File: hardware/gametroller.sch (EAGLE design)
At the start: 48 parts, among them J1 microUSB, J2 PJ-002AH-SMT-TR, J3 USB-A, SW1 SPST_TACT-KMR2, U1 LP5907MFX-3.3/NOPB, U16 AOZ1280CI, U2 TPS2115AIPWRQ1-SON8, U4 ATSAMD21G18_QFN, X2 32.768

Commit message: Minor modifications and cleanup to PCB
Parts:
- added F1: 500mA, gametroller:R-US_R0603
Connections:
- new net N$4: F1.1, J1.VBUS
- net VBUS: now also F1.2; no longer J1.VBUS
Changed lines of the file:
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@@
 <?xml version="1.0" encoding="utf-8"?>
 <!DOCTYPE eagle SYSTEM "eagle.dtd">
-<eagle version="9.1.0">
+<eagle version="9.1.3">
 <drawing>
 <settings>
@@
 <part name="SW1" library="gametroller" deviceset="SPST_TACT" device="-KMR2"/>
 <part name="+3V4" library="gametroller" deviceset="+3V3" device=""/>
-<part name="U$1" library="gametroller" deviceset="VBUS" device=""/>
 <part name="J1" library="gametroller" deviceset="USB-MICRO" device="" value="microUSB"/>
 <part name="U4" library="gametroller" deviceset="ATSAMD21J" device="_QFP" value="ATSAMD21G18_QFN"/>
@@
 <part name="R3" library="gametroller" deviceset="R-US_" device="R0603" value="1k"/>
 <part name="GND3" library="gametroller" deviceset="GND" device=""/>
+<part name="F1" library="gametroller" deviceset="R-US_" device="R0603" value="500mA">
+<attribute name="MFG" value="Bel Fuse Inc."/>
+<attribute name="MPN" value="0ZCK0050FF2E"/>
+<attribute name="PN-DK" value="507-1813-1-ND"/>
+</part>
+<part name="U$2" library="gametroller" deviceset="VBUS" device=""/>
 </parts>
 <sheets>
@@
 </instance>
 <instance part="+3V4" gate="G$1" x="66.04" y="147.32" rot="MR0"/>
-<instance part="U$1" gate="G$1" x="162.56" y="63.5"/>
 <instance part="J1" gate="G$1" x="149.86" y="53.34" rot="MR0"/>
 <instance part="U4" gate="G$1" x="60.96" y="60.96"/>
@@
 <instance part="R3" gate="G$1" x="213.36" y="60.96" rot="R270"/>
 <instance part="GND3" gate="G$1" x="213.36" y="40.64" rot="MR0"/>
+<instance part="F1" gate="G$1" x="165.1" y="58.42" smashed="yes">
+<attribute name="NAME" x="162.56" y="60.96" size="1.778" layer="95" align="center"/>
+<attribute name="VALUE" x="170.18" y="60.96" size="1.778" layer="96" align="center"/>
+<attribute name="MFG" x="165.1" y="58.42" size="1.778" layer="96" display="off"/>
+</instance>
+<instance part="U$2" gate="G$1" x="180.34" y="63.5"/>
 </instances>
 <busses>
@@
 <net name="VBUS" class="0">
 <segment>
-<wire x1="157.48" y1="58.42" x2="162.56" y2="58.42" width="0.1524" layer="91"/>
-<wire x1="162.56" y1="58.42" x2="162.56" y2="60.96" width="0.1524" layer="91"/>
-<pinref part="U$1" gate="G$1" pin="VBUS"/>
-<pinref part="J1" gate="G$1" pin="VBUS"/>
-<wire x1="162.56" y1="58.42" x2="180.34" y2="58.42" width="0.1524" layer="91"/>
-<junction x="162.56" y="58.42"/>
 <pinref part="C18" gate="G$1" pin="1"/>
+<wire x1="170.18" y1="58.42" x2="180.34" y2="58.42" width="0.1524" layer="91"/>
 <wire x1="180.34" y1="58.42" x2="180.34" y2="55.88" width="0.1524" layer="91"/>
+<pinref part="F1" gate="G$1" pin="2"/>
+<pinref part="U$2" gate="G$1" pin="VBUS"/>
+<wire x1="180.34" y1="58.42" x2="180.34" y2="60.96" width="0.1524" layer="91"/>
+<junction x="180.34" y="58.42"/>
 </segment>
 <segment>
@@
 <segment>
 <pinref part="J3" gate="G$1" pin="D+"/>
-<wire x1="160.02" y1="86.36" x2="170.18" y2="86.36" width="0.1524" layer="91"/>
-<label x="165.1" y="86.36" size="1.778" layer="95"/>
+<wire x1="160.02" y1="83.82" x2="170.18" y2="83.82" width="0.1524" layer="91"/>
+<label x="165.1" y="83.82" size="1.778" layer="95"/>
 </segment>
 </net>
@@
 <segment>
 <pinref part="J3" gate="G$1" pin="D-"/>
-<wire x1="160.02" y1="83.82" x2="170.18" y2="83.82" width="0.1524" layer="91"/>
-<label x="165.1" y="83.82" size="1.778" layer="95"/>
+<wire x1="160.02" y1="86.36" x2="170.18" y2="86.36" width="0.1524" layer="91"/>
+<label x="165.1" y="86.36" size="1.778" layer="95"/>
 </segment>
 </net>
@@
 </segment>
 </net>
+<net name="N$4" class="0">
+<segment>
+<pinref part="F1" gate="G$1" pin="1"/>
+<wire x1="157.48" y1="58.42" x2="160.02" y2="58.42" width="0.1524" layer="91"/>
+<pinref part="J1" gate="G$1" pin="VBUS"/>
+</segment>
+</net>

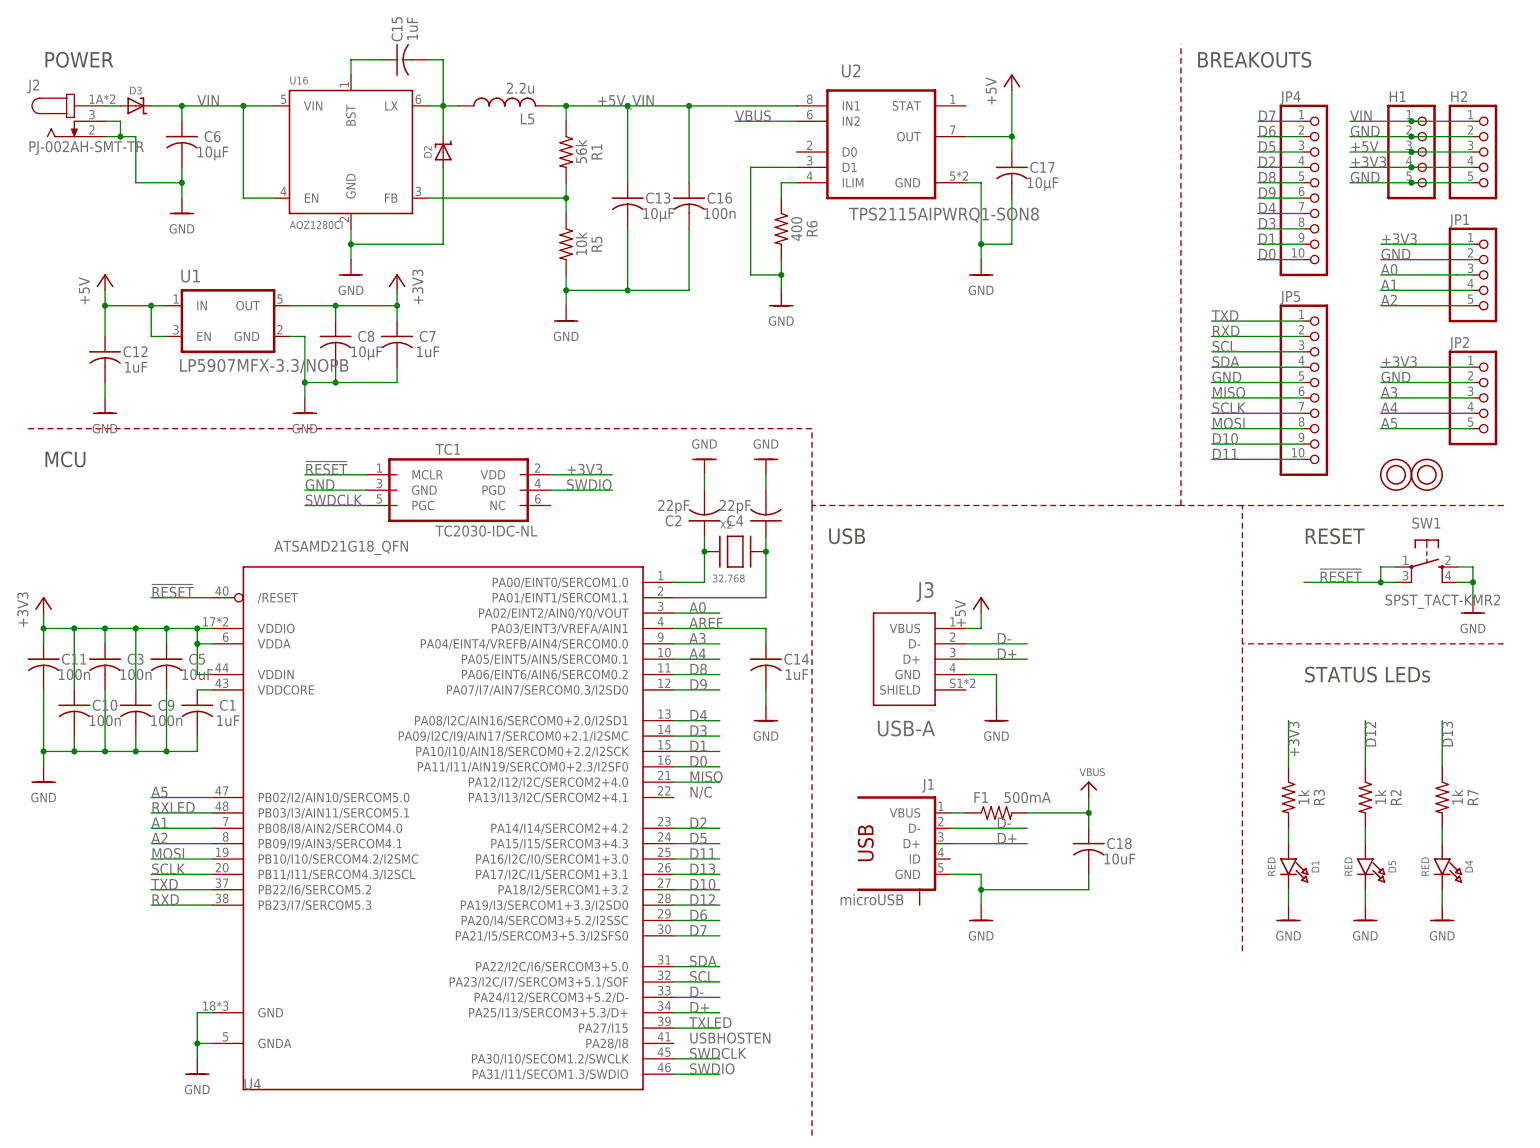
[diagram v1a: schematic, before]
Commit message: Added 22M pullup resistors to several IO pins to allow board to be used as a MaKeyMaKey clone
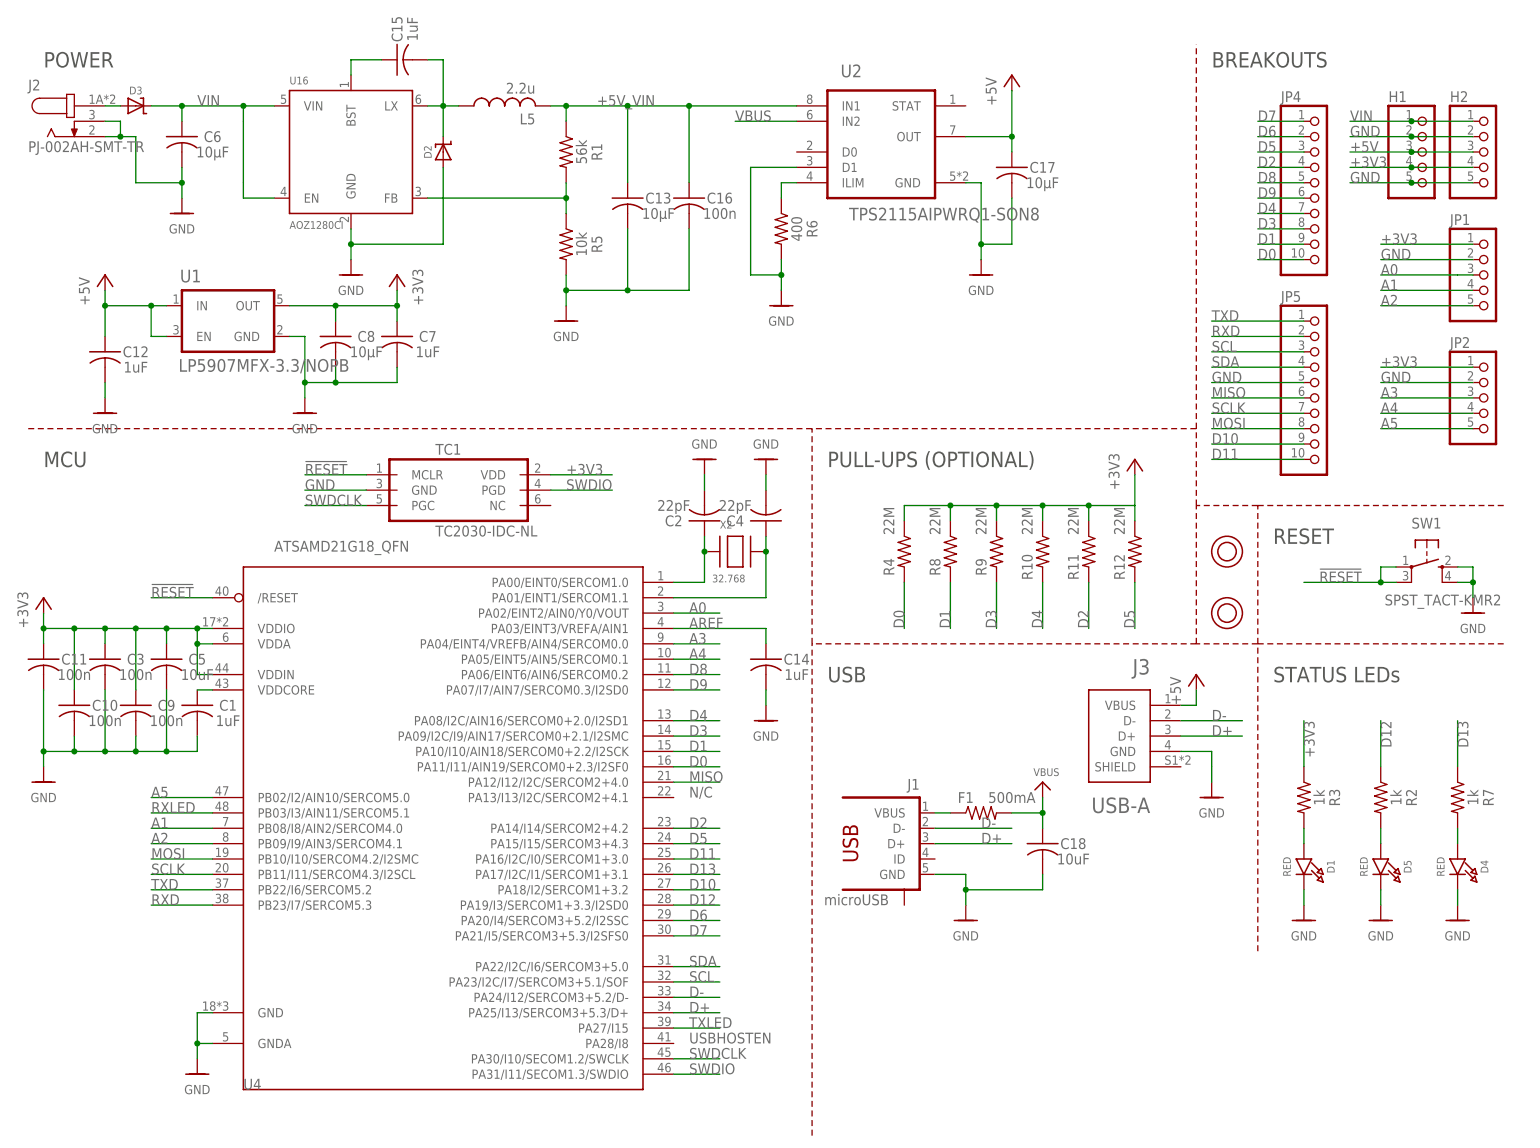
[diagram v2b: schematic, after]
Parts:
- added R10, R11, R12, R4, R8, R9: 22M, gametroller:R-US_R0603
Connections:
- net +3V3: now also R10.1, R11.1, R12.1, R4.1, R8.1, R9.1
- net D0: now also R4.2
- net D1: now also R8.2
- net D2: now also R11.2
- net D3: now also R9.2
- net D4: now also R10.2
- net D5: now also R12.2
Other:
- note added: "PULL-UPS (OPTIONAL)"
- moved on the sheet: C18, D1, D4, D5, F1, J1, J3, R2, R3, R7

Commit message: Updated BOM attributes for currently available parts
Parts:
- C1, C12, C14, C15, C7: MFG (none) -> AVX Corporation; MPN (none) -> 0603ZC105KAT2A; PN-DK (none) -> 478-7940-1-ND
- C10, C11, C16, C3, C9: MFG (none) -> KEMET; MPN (none) -> C0603X104K5RAC7867; PN-DK (none) -> 399-7969-1-ND
- C13, C17, C6, C8: value 10µF -> 10uF; MFG (none) -> TDK Corporation; MPN (none) -> C2012JB1E106K085AC; PN-DK (none) -> 445-11462-1-ND
- C18, C5: MFG (none) -> TDK Corporation; MPN (none) -> C2012JB1E106K085AC; PN-DK (none) -> 445-11462-1-ND
- C2, C4: MFG (none) -> KEMET; MPN (none) -> C0603C220K4GACTU; PN-DK (none) -> 399-9031-1-ND
- D1, D4, D5: MFG (none) -> Lite-On Inc.; MPN (none) -> LTST-C170GKT; PN-DK (none) -> 160-1179-1-ND
- D2, D3: value (none) -> 30V, 2A
- J1: value microUSB -> USB-MICRO
- L5: MFG (none) -> Laird-Signal Integrity Products; MPN (none) -> TYS50402R2N-10
- R1: MFG (none) -> Panasonic Electronic Components; MPN (none) -> ERJ-3EKF5602V; PN-DK (none) -> P56.0KHCT-ND
- R10, R11, R12, R4, R8, R9: MFG (none) -> Panasonic Electronic Components; MPN (none) -> ERJ-3GEYK226V; PN-DK (none) -> P22MGCT-ND
- R2, R3, R7: MFG (none) -> Panasonic Electronic Components; MPN (none) -> ERJ-3EKF1001V; PN-DK (none) -> P1.00KHCT-ND
- R5: MFG (none) -> Panasonic Electronic Components; MPN (none) -> ERJ-3GEYJ103V; PN-DK (none) -> P10KGCT-ND
- R6: MFG (none) -> Panasonic Electronic Components; MPN (none) -> ERJ-2RKF4020X; PN-DK (none) -> P402LCT-ND
- SW1: MFG (none) -> C&K; MPN (none) -> KMR211GLFS; PN-DK (none) -> 401-1426-1-ND
- U4: value ATSAMD21G18_QFN -> ATSAMD21G18
- X2: MFG (none) -> ECS Inc.; MPN (none) -> ECS-.327-12.5-34B-TR; PN-DK (none) -> XC1617CT-ND
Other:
- moved on the sheet: D3, JP1, JP2

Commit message: Minor hardware tweaks
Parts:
- F1: MFG Bel Fuse Inc. -> Bourns Inc.; MPN 0ZCK0050FF2E -> MF-FSMF050X-2; PN-DK 507-1813-1-ND -> MF-FSMF050X-2CT-ND
- R6: MPN ERJ-2RKF4020X -> ERJ-3EKF4020V; PN-DK P402LCT-ND -> P402HCT-ND
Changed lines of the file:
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@@
 <grid distance="0.1" unitdist="inch" unit="inch" style="dots" multiple="1" display="yes" altdistance="0.01" altunitdist="inch" altunit="inch"/>
 <layers>
-<layer number="1" name="Top" color="4" fill="1" visible="yes" active="no"/>
-<layer number="2" name="Route2" color="1" fill="3" visible="yes" active="no"/>
-<layer number="3" name="Route3" color="4" fill="3" visible="yes" active="no"/>
-<layer number="4" name="Route4" color="1" fill="4" visible="yes" active="no"/>
-<layer number="5" name="Route5" color="4" fill="4" visible="yes" active="no"/>
-<layer number="6" name="Route6" color="1" fill="8" visible="yes" active="no"/>
-<layer number="7" name="Route7" color="4" fill="8" visible="yes" active="no"/>
-<layer number="8" name="Route8" color="1" fill="2" visible="yes" active="no"/>
-<layer number="9" name="Route9" color="4" fill="2" visible="yes" active="no"/>
-<layer number="10" name="Route10" color="1" fill="7" visible="yes" active="no"/>
-<layer number="11" name="Route11" color="4" fill="7" visible="yes" active="no"/>
-<layer number="12" name="Route12" color="1" fill="5" visible="yes" active="no"/>
-<layer number="13" name="Route13" color="4" fill="5" visible="yes" active="no"/>
-<layer number="14" name="Route14" color="1" fill="6" visible="yes" active="no"/>
-<layer number="15" name="Route15" color="4" fill="6" visible="yes" active="no"/>
-<layer number="16" name="Bottom" color="1" fill="1" visible="yes" active="no"/>
-<layer number="17" name="Pads" color="2" fill="1" visible="yes" active="no"/>
-<layer number="18" name="Vias" color="2" fill="1" visible="yes" active="no"/>
-<layer number="19" name="Unrouted" color="6" fill="1" visible="yes" active="no"/>
-<layer number="20" name="Dimension" color="11" fill="1" visible="yes" active="no"/>
-<layer number="21" name="tPlace" color="14" fill="1" visible="yes" active="no"/>
-<layer number="22" name="bPlace" color="13" fill="1" visible="yes" active="no"/>
-<layer number="23" name="tOrigins" color="14" fill="1" visible="yes" active="no"/>
-<layer number="24" name="bOrigins" color="13" fill="1" visible="yes" active="no"/>
-<layer number="25" name="tNames" color="7" fill="1" visible="yes" active="no"/>
-<layer number="26" name="bNames" color="7" fill="1" visible="yes" active="no"/>
-<layer number="27" name="tValues" color="7" fill="1" visible="yes" active="no"/>
-<layer number="28" name="bValues" color="7" fill="1" visible="yes" active="no"/>
+<layer number="1" name="Top" color="4" fill="1" visible="no" active="no"/>
+<layer number="2" name="Route2" color="1" fill="3" visible="no" active="no"/>
+<layer number="3" name="Route3" color="4" fill="3" visible="no" active="no"/>
+<layer number="4" name="Route4" color="1" fill="4" visible="no" active="no"/>
+<layer number="5" name="Route5" color="4" fill="4" visible="no" active="no"/>
+<layer number="6" name="Route6" color="1" fill="8" visible="no" active="no"/>
+<layer number="7" name="Route7" color="4" fill="8" visible="no" active="no"/>
+<layer number="8" name="Route8" color="1" fill="2" visible="no" active="no"/>
+<layer number="9" name="Route9" color="4" fill="2" visible="no" active="no"/>
+<layer number="10" name="Route10" color="1" fill="7" visible="no" active="no"/>
+<layer number="11" name="Route11" color="4" fill="7" visible="no" active="no"/>
+<layer number="12" name="Route12" color="1" fill="5" visible="no" active="no"/>
+<layer number="13" name="Route13" color="4" fill="5" visible="no" active="no"/>
+<layer number="14" name="Route14" color="1" fill="6" visible="no" active="no"/>
+<layer number="15" name="Route15" color="4" fill="6" visible="no" active="no"/>
+<layer number="16" name="Bottom" color="1" fill="1" visible="no" active="no"/>
+<layer number="17" name="Pads" color="2" fill="1" visible="no" active="no"/>
+<layer number="18" name="Vias" color="2" fill="1" visible="no" active="no"/>
+<layer number="19" name="Unrouted" color="6" fill="1" visible="no" active="no"/>
+<layer number="20" name="Dimension" color="11" fill="1" visible="no" active="no"/>
+<layer number="21" name="tPlace" color="14" fill="1" visible="no" active="no"/>
+<layer number="22" name="bPlace" color="13" fill="1" visible="no" active="no"/>
+<layer number="23" name="tOrigins" color="14" fill="1" visible="no" active="no"/>
+<layer number="24" name="bOrigins" color="13" fill="1" visible="no" active="no"/>
+<layer number="25" name="tNames" color="7" fill="1" visible="no" active="no"/>
+<layer number="26" name="bNames" color="7" fill="1" visible="no" active="no"/>
+<layer number="27" name="tValues" color="7" fill="1" visible="no" active="no"/>
+<layer number="28" name="bValues" color="7" fill="1" visible="no" active="no"/>
 <layer number="29" name="tStop" color="7" fill="3" visible="no" active="no"/>
 <layer number="30" name="bStop" color="7" fill="6" visible="no" active="no"/>
@@
 <layer number="35" name="tGlue" color="7" fill="4" visible="no" active="no"/>
 <layer number="36" name="bGlue" color="7" fill="5" visible="no" active="no"/>
-<layer number="37" name="tTest" color="7" fill="1" visible="yes" active="no"/>
-<layer number="38" name="bTest" color="7" fill="1" visible="yes" active="no"/>
+<layer number="37" name="tTest" color="7" fill="1" visible="no" active="no"/>
+<layer number="38" name="bTest" color="7" fill="1" visible="no" active="no"/>
 <layer number="39" name="tKeepout" color="4" fill="11" visible="no" active="no"/>
 <layer number="40" name="bKeepout" color="1" fill="11" visible="no" active="no"/>
@@
 <layer number="44" name="Drills" color="7" fill="1" visible="no" active="no"/>
 <layer number="45" name="Holes" color="7" fill="1" visible="no" active="no"/>
-<layer number="46" name="Milling" color="3" fill="1" visible="yes" active="no"/>
-<layer number="47" name="Measures" color="7" fill="1" visible="yes" active="no"/>
-<layer number="48" name="Document" color="7" fill="1" visible="yes" active="no"/>
-<layer number="49" name="Reference" color="7" fill="1" visible="yes" active="no"/>
-<layer number="50" name="dxf" color="7" fill="1" visible="yes" active="no"/>
-<layer number="51" name="tDocu" color="7" fill="1" visible="yes" active="no"/>
-<layer number="52" name="bDocu" color="7" fill="1" visible="yes" active="no"/>
-<layer number="53" name="tGND_GNDA" color="7" fill="9" visible="yes" active="no"/>
-<layer number="54" name="bGND_GNDA" color="1" fill="9" visible="yes" active="no"/>
-<layer number="56" name="wert" color="7" fill="1" visible="yes" active="no"/>
-<layer number="57" name="tCAD" color="7" fill="1" visible="yes" active="no"/>
-<layer number="59" name="tCarbon" color="7" fill="1" visible="yes" active="no"/>
-<layer number="60" name="bCarbon" color="7" fill="1" visible="yes" active="no"/>
+<layer number="46" name="Milling" color="3" fill="1" visible="no" active="no"/>
+<layer number="47" name="Measures" color="7" fill="1" visible="no" active="no"/>
+<layer number="48" name="Document" color="7" fill="1" visible="no" active="no"/>
+<layer number="49" name="Reference" color="7" fill="1" visible="no" active="no"/>
+<layer number="50" name="dxf" color="7" fill="1" visible="no" active="no"/>
+<layer number="51" name="tDocu" color="7" fill="1" visible="no" active="no"/>
+<layer number="52" name="bDocu" color="7" fill="1" visible="no" active="no"/>
+<layer number="53" name="tGND_GNDA" color="7" fill="9" visible="no" active="no"/>
+<layer number="54" name="bGND_GNDA" color="1" fill="9" visible="no" active="no"/>
+<layer number="56" name="wert" color="7" fill="1" visible="no" active="no"/>
+<layer number="57" name="tCAD" color="7" fill="1" visible="no" active="no"/>
+<layer number="59" name="tCarbon" color="7" fill="1" visible="no" active="no"/>
+<layer number="60" name="bCarbon" color="7" fill="1" visible="no" active="no"/>
 <layer number="88" name="SimResults" color="9" fill="1" visible="yes" active="yes"/>
 <layer number="89" name="SimProbes" color="9" fill="1" visible="yes" active="yes"/>
@@
 <part name="R6" library="gametroller" deviceset="R-US_" device="R0603" value="400">
 <attribute name="MFG" value="Panasonic Electronic Components"/>
-<attribute name="MPN" value="ERJ-2RKF4020X"/>
-<attribute name="PN-DK" value="P402LCT-ND"/>
+<attribute name="MPN" value="ERJ-3EKF4020V"/>
+<attribute name="PN-DK" value="P402HCT-ND"/>
 </part>
 <part name="C16" library="gametroller" deviceset="C-US" device="C0603" value="100n">
@@
 <part name="GND3" library="gametroller" deviceset="GND" device=""/>
 <part name="F1" library="gametroller" deviceset="R-US_" device="R0603" value="500mA">
-<attribute name="MFG" value="Bel Fuse Inc."/>
-<attribute name="MPN" value="0ZCK0050FF2E"/>
-<attribute name="PN-DK" value="507-1813-1-ND"/>
+<attribute name="MFG" value="Bourns Inc."/>
+<attribute name="MPN" value="MF-FSMF050X-2 "/>
+<attribute name="PN-DK" value="MF-FSMF050X-2CT-ND "/>
 </part>
 <part name="U$2" library="gametroller" deviceset="VBUS" device=""/>
